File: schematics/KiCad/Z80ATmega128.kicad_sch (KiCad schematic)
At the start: 89 parts, among them J1 AVR-ISP-6, J2 Serial I/O, J3 DC 5V, J4 DC 5V, J5 Z80[1..20], J6 Micro_SD_Card_Det_Hirose_DM3AT, J7 Z80[21..40], SW1 RESET, SW2 POWER, U1 74HC08, U10 74HC32, U11 74HC4050, U12 LP2950-3.3, U13 74HC74, U2 74HC04, U3 74HC125, U4 74AC573, U5 74HC574, U6 74HC125, U7 74HC244, U8 74HC245, U9 74HC32, Y1 16MHz, Y2 8MHz

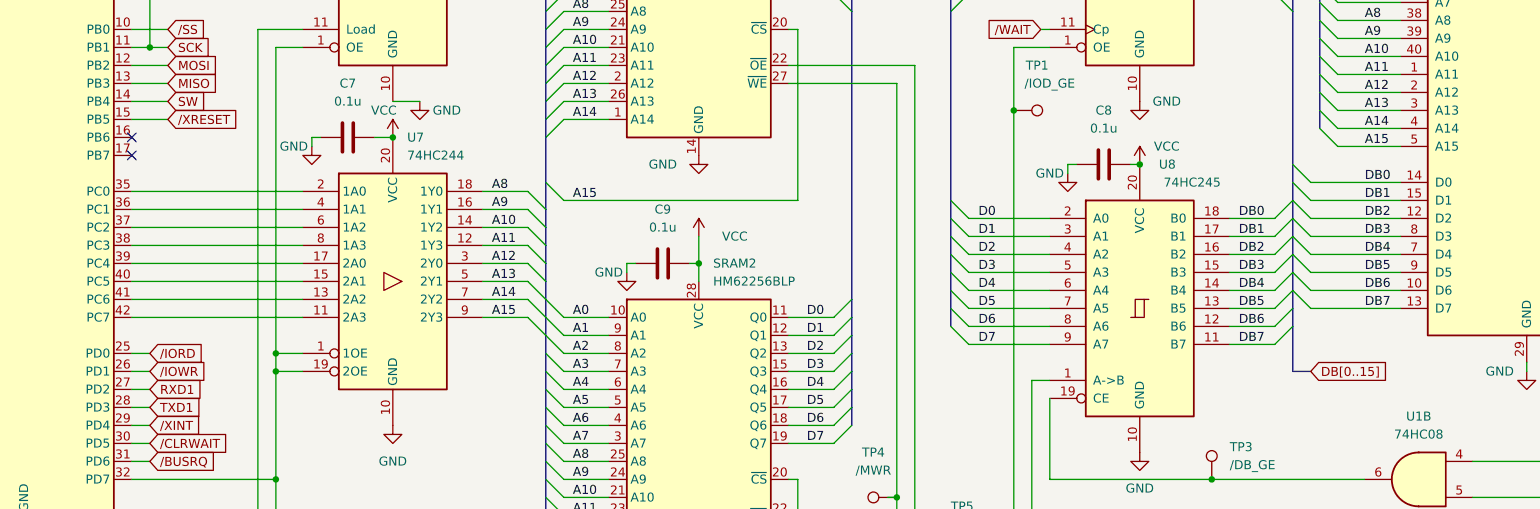
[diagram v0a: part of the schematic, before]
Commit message: Update schematics for Z80 /HALT and /NMI.
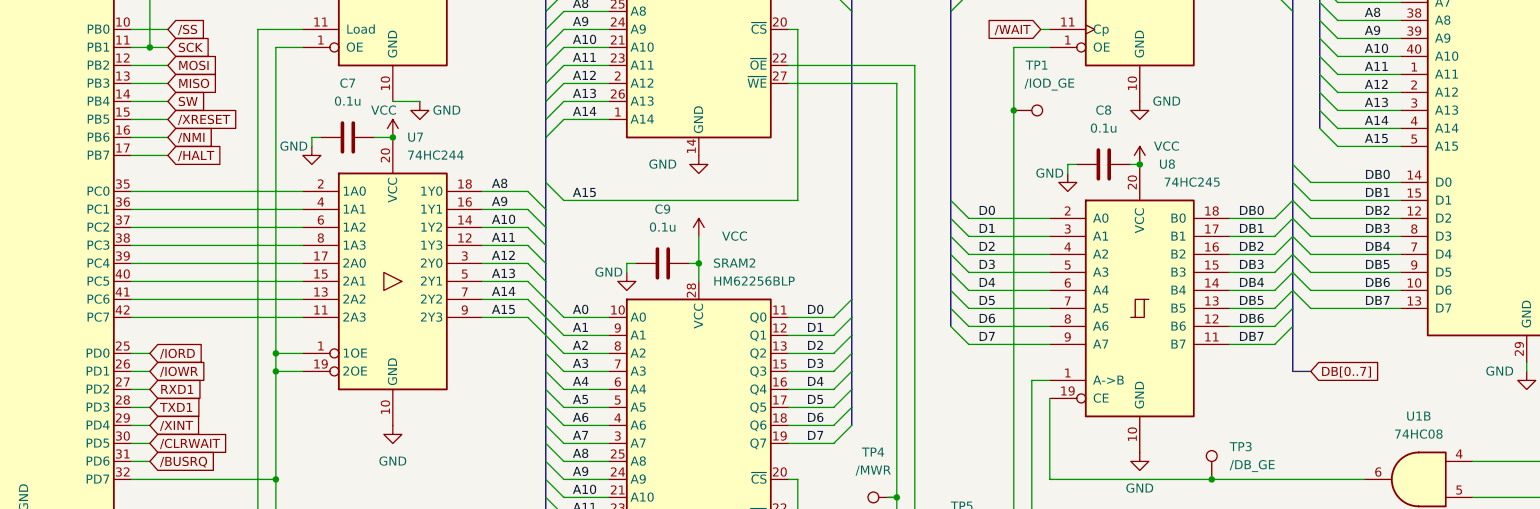
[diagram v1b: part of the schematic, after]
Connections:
- net /HALT: now also CPU2.17 (PB7)
- net /NMI: now also CPU2.16 (PB6)
- no-connect marks 17 -> 15
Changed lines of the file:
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@@
   )
   (no_connect (at 289.56 259.08))
-  (no_connect (at 135.89 86.36))
-  (no_connect (at 135.89 83.82))
   (no_connect (at 105.41 78.74))
   (no_connect (at 289.56 273.05))
@@
     (stroke (width 0) (type default) (color 0 0 0 0))
   )
+  (wire (pts (xy 135.89 83.82) (xy 140.97 83.82))
+    (stroke (width 0) (type default) (color 0 0 0 0))
+  )
   (wire (pts (xy 261.62 205.74) (xy 261.62 212.09))
     (stroke (width 0) (type default) (color 0 0 0 0))
@@
     (stroke (width 0) (type default) (color 0 0 0 0))
   )
+  (wire (pts (xy 135.89 86.36) (xy 140.97 86.36))
+    (stroke (width 0) (type default) (color 0 0 0 0))
+  )
   (wire (pts (xy 394.97 26.67) (xy 394.97 30.48))
     (stroke (width 0) (type default) (color 0 0 0 0))
@@
     )
   )
+  (global_label "{slash}NMI" (shape input) (at 140.97 83.82 0) (fields_autoplaced)
+    (effects (font (size 1.27 1.27)) (justify left))
+    (property "シート間のリファレンス" "${INTERSHEET_REFS}" (id 0) (at 148.1002 83.7406 0)
+      (effects (font (size 1.27 1.27)) (justify left) hide)
+    )
+  )
   (global_label "{slash}IORD" (shape input) (at 138.43 114.3 0) (fields_autoplaced)
     (effects (font (size 1.27 1.27)) (justify left))
@@
     )
   )
-  (global_label "DB[0..15]" (shape input) (at 302.26 116.84 0) (fields_autoplaced)
+  (global_label "DB[0..7]" (shape input) (at 302.26 116.84 0) (fields_autoplaced)
     (effects (font (size 1.27 1.27)) (justify left))
-    (property "シート間のリファレンス" "${INTERSHEET_REFS}" (id 0) (at 313.7445 116.7606 0)
+    (property "シート間のリファレンス" "${INTERSHEET_REFS}" (id 0) (at 312.535 116.7606 0)
       (effects (font (size 1.27 1.27)) (justify left) hide)
     )
@@
       (effects (font (size 1.27 1.27)) (justify left) hide)
     )
+  )
+  (global_label "{slash}HALT" (shape input) (at 140.97 86.36 0) (fields_autoplaced)
+    (effects (font (size 1.27 1.27)) (justify left))
+    (property "シート間のリファレンス" "${INTERSHEET_REFS}" (id 0) (at 149.1283 86.2806 0)
+      (effects (font (size 1.27 1.27)) (justify left) hide)
+    )

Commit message: Update schematics.
Separate reset and SD card interface as different layer.
Power on/manual reset are isolated from ISP /RST for stability.
XMEM /RD(PG1) and /WR(PG0) were swapped.
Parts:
- removed C22: 0.1u, Capacitor_THT:C_Disc_D3.8mm_W2.6mm_P2.50mm, symbol Device:C
- removed C6: 1u, Capacitor_THT:CP_Radial_Tantal_D5.0mm_P2.50mm, symbol Device:C
- removed D2: 1N4148, Diode_THT:D_DO-35_SOD27_P7.62mm_Horizontal, symbol Diode:1N4148
- removed D4: SD Access, LED_THT:LED_D3.0mm, symbol Device:LED
- removed J6: Micro_SD_Card_Det_Hirose_DM3AT, Connector_Card:microSD_HC_Hirose_DM3AT-SF-PEJM5, symbol Connector:Micro_SD_Card_Det_Hirose_DM3AT
- removed R15, R16, R17, R2, R21, R3: 10K, Resistor_THT:R_Axial_DIN0204_L3.6mm_D1.6mm_P7.62mm_Horizontal, symbol Device:R
- removed R22: 1K, Resistor_THT:R_Axial_DIN0204_L3.6mm_D1.6mm_P7.62mm_Horizontal, symbol Device:R
- removed R4: 100, Resistor_THT:R_Axial_DIN0204_L3.6mm_D1.6mm_P7.62mm_Horizontal, symbol Device:R
- removed SW1: RESET, Button_Switch_THT:SW_PUSH_6mm_H7.3mm, symbol Switch:SW_Push
- removed unit 4 of U1
- removed U11: 74HC4050, Package_DIP:DIP-16_W7.62mm, symbol 4xxx:4050
- added JP1: Disable Z80, Connector_PinHeader_2.54mm:PinHeader_1x03_P2.54mm_Vertical, symbol Jumper:Jumper_3_Open
- added R1: 10K, Resistor_THT:R_Axial_DIN0204_L3.6mm_D1.6mm_P7.62mm_Horizontal, symbol Device:R
- D2: renamed from D1; value DMA -> Z80 active
- J4: renamed from J5; symbol Connector:Conn_01x20_Male -> Connector:Conn_01x20_Pin
- J6: renamed from J7; symbol Connector:Conn_01x20_Male -> Connector:Conn_01x20_Pin
- SRAM1, SRAM2: footprint Package_DIP:DIP-28_W15.24mm -> Package_DIP:DIP-28_W15.24mm_Socket
- U1: renamed from U3; footprint Package_DIP:DIP-14_W7.62mm -> Package_DIP:DIP-14_W7.62mm_Socket
- U10: footprint Package_DIP:DIP-14_W7.62mm -> Package_DIP:DIP-14_W7.62mm_Socket
- U11: renamed from U13; footprint Package_DIP:DIP-14_W7.62mm -> Package_DIP:DIP-14_W7.62mm_Socket
- U2: renamed from U4; footprint Package_DIP:DIP-20_W7.62mm -> Package_DIP:DIP-20_W7.62mm_Socket
- U3: renamed from U5; footprint Package_DIP:DIP-20_W7.62mm -> Package_DIP:DIP-20_W7.62mm_Socket
- U4: renamed from U2; footprint Package_DIP:DIP-14_W7.62mm -> Package_DIP:DIP-16_W7.62mm_Socket
- U5: renamed from U6; footprint Package_DIP:DIP-14_W7.62mm -> Package_DIP:DIP-14_W7.62mm_Socket
- U6: renamed from U7; footprint Package_DIP:DIP-20_W7.62mm -> Package_DIP:DIP-20_W7.62mm_Socket
- U7: renamed from U8; footprint Package_DIP:DIP-20_W7.62mm -> Package_DIP:DIP-20_W7.62mm_Socket
- U8: renamed from U9; footprint Package_DIP:DIP-14_W7.62mm -> Package_DIP:DIP-14_W7.62mm_Socket
- U9: renamed from U1; footprint Package_DIP:DIP-14_W7.62mm -> Package_DIP:DIP-14_W7.62mm_Socket
- renumbered C13 to C10, C14 to C11, C11 to C12, C12 to C13, C15 to C14, C16 to C15, C17 to C16, C18 to C17, C19 to C18, C20 to C19, C21 to C20, C7 to C6, C8 to C7, C9 to C8, C10 to C9, D3 to D1, J4 to J5, JP1 to JP2, R13 to R10, R14 to R11, R20 to R12, R18 to R13, R19 to R14, R1 to R15, R5 to R2, R6 to R3, R7 to R4, R8 to R5, R9 to R6, R10 to R7, R11 to R8, R12 to R9, SW2 to SW1, TP12 to TP10, TP9 to TP12, TP7 to TP6, TP6 to TP7, TP10 to TP8, TP8 to TP9
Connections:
- net GND: now also JP1.1 (A)
- net VCC: now also R1.1
- net /BUSRQ: now also JP1.3 (B); no longer CPU1.25 (~{BUSRQ}), R9.2
- net /RD: now also U5.12; no longer U5.9
- net /WR: now also U5.9; no longer U5.12
- net at SRAM1.22 (~{OE}), SRAM2.22 (~{OE}), TP5.1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: now also U5.11; no longer U5.8
- net at SRAM1.27 (~{WE}), SRAM2.27 (~{WE}), TP4.1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: now also U5.8; no longer U5.11
- net Reset//ISP_RST: now reaches J1.5 (~{RST}), U1.13, U4.5
- net Reset//ISP_RST: now also R1.2; no longer CPU2.20 (~{RESET})
- net /RESET renamed /Z80_RESET
- net /XRESET renamed Reset//Z80_SWRST
- new net: CPU1.25 (~{BUSRQ}), JP1.2 (C), R9.2
- new net Reset//AVR_RST: CPU2.20 (~{RESET})
- no-connect marks 15 -> 10
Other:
- added sheet Reset (Reset.kicad_sch)
- added sheet SD_Card_Interface (SD_Card.kicad_sch)
- title: (none) -> Z80 / ATmega128 Board
- moved on the sheet: C10, C11, C12, C13, C9, D1, D2, J3, J4, J5, J6, JP2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

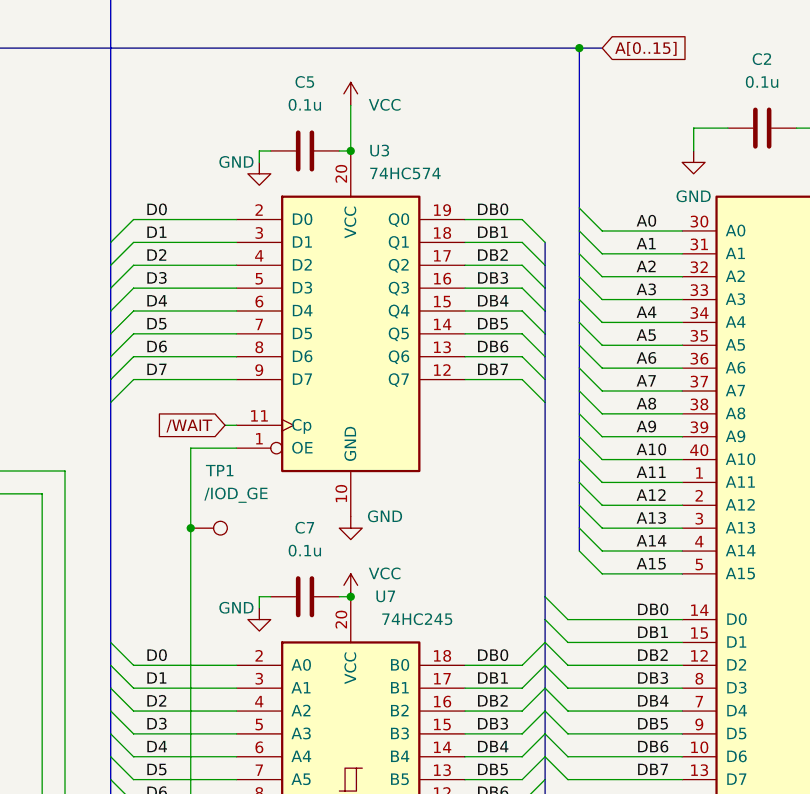
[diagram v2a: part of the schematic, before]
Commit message: 74HC574 and 245 are changed to 74HCT.
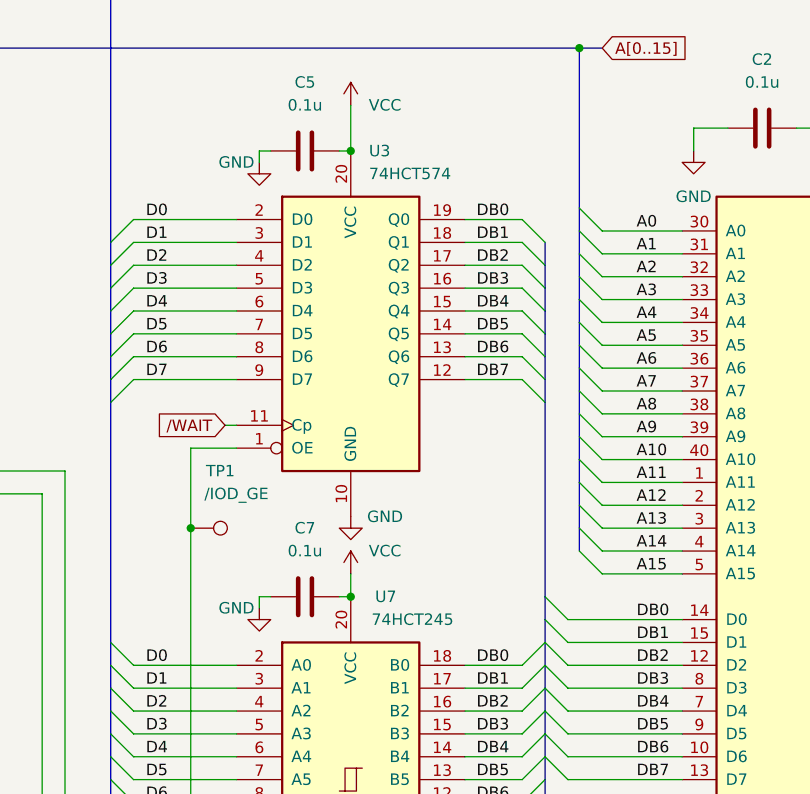
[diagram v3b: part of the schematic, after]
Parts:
- U3: value 74HC574 -> 74HCT574
- U7: value 74HC245 -> 74HCT245
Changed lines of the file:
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@@
     (stroke (width 0) (type default))
   )
+  (wire (pts (xy 278.13 85.09) (xy 278.13 87.63))
+    (stroke (width 0) (type default))
+  )
   (bus (pts (xy 91.44 109.22) (xy 91.44 111.76))
     (stroke (width 0) (type default))
@@
       (effects (font (size 1.27 1.27)) (justify right))
     )
-    (property "Value" "74HC245" (at 289.56 90.17 0)
+    (property "Value" "74HCT245" (at 289.56 90.17 0)
       (effects (font (size 1.27 1.27)) (justify right))
     )
@@
       (effects (font (size 1.27 1.27)) hide)
     )
-    (property "Datasheet" "http://www.ti.com/lit/gpn/sn74HC245" (at 278.13 107.95 0)
+    (property "Datasheet" "http://www.ti.com/lit/gpn/sn74HCT245" (at 278.13 107.95 0)
       (effects (font (size 1.27 1.27)) hide)
     )
@@
     )
   )
-  (symbol (lib_id "power:VCC") (at 278.13 87.63 0) (unit 1)
+  (symbol (lib_id "power:VCC") (at 278.13 85.09 0) (unit 1)
     (in_bom yes) (on_board yes) (dnp no)
-    (property "Reference" "#PWR026" (at 278.13 91.44 0)
+    (property "Reference" "#PWR026" (at 278.13 88.9 0)
       (effects (font (size 1.27 1.27)) hide)
     )
-    (property "Value" "VCC" (at 281.94 85.09 0)
+    (property "Value" "VCC" (at 281.94 82.55 0)
       (effects (font (size 1.27 1.27)))
     )
-    (property "Footprint" "" (at 278.13 87.63 0)
+    (property "Footprint" "" (at 278.13 85.09 0)
       (effects (font (size 1.27 1.27)) hide)
     )
-    (property "Datasheet" "" (at 278.13 87.63 0)
+    (property "Datasheet" "" (at 278.13 85.09 0)
       (effects (font (size 1.27 1.27)) hide)
     )
@@
       (effects (font (size 1.27 1.27)) (justify left))
     )
-    (property "Value" "74HC574" (at 280.1494 40.64 0)
+    (property "Value" "74HCT574" (at 280.1494 40.64 0)
       (effects (font (size 1.27 1.27)) (justify left))
     )
@@
       (effects (font (size 1.27 1.27)) hide)
     )
-    (property "Datasheet" "http://www.ti.com/lit/gpn/sn74HC574" (at 278.13 58.42 0)
+    (property "Datasheet" "http://www.ti.com/lit/gpn/sn74HCT574" (at 278.13 58.42 0)
       (effects (font (size 1.27 1.27)) hide)
     )

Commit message: Changed USB power line connection.
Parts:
- removed J2: Serial I/O, Connector_PinHeader_2.54mm:PinHeader_1x05_P2.54mm_Vertical, symbol Connector:Screw_Terminal_01x05
- added J2: Serial0, Connector_PinHeader_2.54mm:PinHeader_1x06_P2.54mm_Vertical, symbol Connector:Conn_01x06_Pin
- added J3: Serial1, Connector_PinHeader_2.54mm:PinHeader_1x06_P2.54mm_Vertical, symbol Connector:Conn_01x06_Pin
- U4: footprint Package_DIP:DIP-16_W7.62mm_Socket -> Package_DIP:DIP-14_W7.62mm_Socket
- renumbered J3 to J4, J4 to J5, J5 to J6, J6 to J7
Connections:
- net GND: now also J2.6 (Pin_6), J3.6 (Pin_6)
- net RXD1: now also J3.2 (Pin_2)
- net TXD1: now also J3.3 (Pin_3)
- net at U5.2: now also J2.2 (Pin_2)
- net at U5.6: now also J2.3 (Pin_3)
- net VBUS: now reaches JP2.2 (C), SW1.2 (B)
- net VBUS: now also J2.4 (Pin_4), J3.4 (Pin_4)
- no-connect marks 10 -> 14
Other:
- moved on the sheet: C12, C13, C9, D1, J4, J6, JP2, R11, SW1, TP12, TP7, TP9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

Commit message: Update Reset circuit and Serial interface
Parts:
- removed C12: 1u, Capacitor_THT:CP_Radial_Tantal_D5.0mm_P2.50mm, symbol Device:C
- removed C13: 1u, Capacitor_THT:CP_Radial_Tantal_D5.0mm_P2.50mm, symbol Device:C_Polarized
- removed J2: Serial0, Connector_PinHeader_2.54mm:PinHeader_1x06_P2.54mm_Vertical, symbol Connector:Conn_01x06_Pin
- removed J3: Serial1, Connector_PinHeader_2.54mm:PinHeader_1x06_P2.54mm_Vertical, symbol Connector:Conn_01x06_Pin
- removed TP12: 3.3V, TestPoint:TestPoint_Loop_D2.50mm_Drill1.0mm, symbol Connector:TestPoint
- removed U12: LP2950-3.3, Package_TO_SOT_THT:TO-92_Inline, symbol Regulator_Linear:LP2950-3.3_TO92
- added U10, U5: AE-CH340E-TYPEC, Connector_PinHeader_2.54mm:PinHeader_1x06_P2.54mm_Vertical, symbol 46nori_Library:AE-CH340E-TYPEC
- renumbered C14 to C12, C15 to C13, C16 to C14, C17 to C15, C18 to C16, C19 to C17, C20 to C18, J4 to J2, J6 to J3, J5 to J4, J7 to J5, TP9 to TP8, TP8 to TP9, U9 to U11, U10 to U12, U11 to U13, U5 to U6, U6 to U7, U7 to U8, U8 to U9
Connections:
- net GND: now also U10.6 (GND), U5.6 (GND)
- net RXD1: now also U10.3 (TXD)
- net TXD1: now also U10.2 (RXD)
- net at U6.2: now also U5.3 (TXD)
- net at U6.6: now also U5.2 (RXD)
- net VBUS: no longer names the net of JP2.2 (C), SW1.2 (B)
- net VBUS: now also U10.4 (VCC), U5.4 (VCC)
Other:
- sheet Reset ports: added /ST; removed none
- moved on the sheet: C9, D1, J2, J3, JP2, R11, SW1, TP7, TP8

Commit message: Update schematics.
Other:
- company: (none) -> By 46nori
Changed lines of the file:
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@@
   (title_block
     (title "Z80 / ATmega128 Board")
-    (date "2023-04-14")
+    (date "2023-05-03")
+    (company "By 46nori")
   )
   (junction (at 389.89 163.83) (diameter 0) (color 0 0 0 0)
@@
     (stroke (width 0) (type default))
   )
+  (wire (pts (xy 34.29 146.05) (xy 43.18 146.05))
+    (stroke (width 0) (type default))
+  )
   (wire (pts (xy 332.74 116.84) (xy 332.74 115.57))
     (stroke (width 0) (type default))
@@
     (stroke (width 0) (type default))
   )
+  (wire (pts (xy 30.48 146.05) (xy 34.29 146.05))
+    (stroke (width 0) (type default))
+  )
   (wire (pts (xy 67.31 116.84) (xy 105.41 116.84))
     (stroke (width 0) (type default))
@@
     (stroke (width 0) (type default))
   )
-  (wire (pts (xy 34.29 146.05) (xy 34.29 149.86))
+  (wire (pts (xy 43.18 146.05) (xy 43.18 149.86))
     (stroke (width 0) (type default))
   )
@@
     (stroke (width 0) (type default))
   )
-  (wire (pts (xy 30.48 146.05) (xy 34.29 146.05))
-    (stroke (width 0) (type default))
-  )
   (wire (pts (xy 142.24 220.98) (xy 142.24 227.33))
     (stroke (width 0) (type default))
@@
     (stroke (width 0) (type default))
   )
+  (text_box "1-2 : Force disable\n2-3 : Enable"
+    (at 383.54 20.32 0) (size 22.86 5.08)
+    (stroke (width 0) (type default))
+    (fill (type none))
+    (effects (font (size 1.27 1.27)) (justify left top))
+  )
+  (text_box "USB/Serial CH0"
+    (at 13.97 114.3 0) (size 17.78 3.81)
+    (stroke (width 0) (type default))
+    (fill (type none))
+    (effects (font (size 1.27 1.27)) (justify top))
+  )
+  (text_box "USB/Serial CH1"
+    (at 13.97 149.86 0) (size 17.78 3.81)
+    (stroke (width 0) (type default))
+    (fill (type none))
+    (effects (font (size 1.27 1.27)) (justify top))
+  )
   (label "D3" (at 231.14 116.84 0) (fields_autoplaced)
     (effects (font (size 1.27 1.27)) (justify left bottom))
@@
     )
   )
-  (symbol (lib_id "power:GND") (at 34.29 149.86 0) (unit 1)
+  (symbol (lib_id "power:GND") (at 43.18 149.86 0) (unit 1)
     (in_bom yes) (on_board yes) (dnp no) (fields_autoplaced)
-    (property "Reference" "#PWR035" (at 34.29 156.21 0)
+    (property "Reference" "#PWR035" (at 43.18 156.21 0)
       (effects (font (size 1.27 1.27)) hide)
     )
-    (property "Value" "GND" (at 34.29 154.94 0)
+    (property "Value" "GND" (at 43.18 154.94 0)
       (effects (font (size 1.27 1.27)))
     )
-    (property "Footprint" "" (at 34.29 149.86 0)
+    (property "Footprint" "" (at 43.18 149.86 0)
       (effects (font (size 1.27 1.27)) hide)
     )
-    (property "Datasheet" "" (at 34.29 149.86 0)
+    (property "Datasheet" "" (at 43.18 149.86 0)
       (effects (font (size 1.27 1.27)) hide)
     )
@@
   (symbol (lib_id "power:PWR_FLAG") (at 38.1 182.88 0) (mirror x) (unit 1)
     (in_bom yes) (on_board yes) (dnp no)
-    (property "Reference" "#FLG01" (at 38.1 184.785 0)
+    (property "Reference" "#FLG02" (at 38.1 184.785 0)
       (effects (font (size 1.27 1.27)) hide)
     )
@@
       (project "Z80ATmega128"
         (path "/8c0ff608-9e5b-458c-8fa7-b9973ff97e88"
-          (reference "#FLG01") (unit 1)
+          (reference "#FLG02") (unit 1)
         )
       )
@@
   (symbol (lib_id "power:PWR_FLAG") (at 68.58 167.64 0) (mirror y) (unit 1)
     (in_bom yes) (on_board yes) (dnp no)
-    (property "Reference" "#FLG02" (at 68.58 165.735 0)
+    (property "Reference" "#FLG01" (at 68.58 165.735 0)
       (effects (font (size 1.27 1.27)) hide)
     )
@@
       (project "Z80ATmega128"
         (path "/8c0ff608-9e5b-458c-8fa7-b9973ff97e88"
-          (reference "#FLG02") (unit 1)
+          (reference "#FLG01") (unit 1)
         )
       )

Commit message: Update RESET circuit using DS1232N.
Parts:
- removed R15: 1K, Resistor_THT:R_Axial_DIN0204_L3.6mm_D1.6mm_P7.62mm_Horizontal, symbol Device:R
- removed SW1: POWER, Button_Switch_THT:SW_Slide_1P2T_CK_OS102011MS2Q, symbol Switch:SW_SPDT
- removed TP1: /IOD_GE, TestPoint:TestPoint_Loop_D2.50mm_Drill1.0mm, symbol Connector:TestPoint
- removed TP10: /CLRWAIT, TestPoint:TestPoint_Loop_D2.50mm_Drill1.0mm, symbol Connector:TestPoint
- removed TP2: /IOWR, TestPoint:TestPoint_Loop_D2.50mm_Drill1.0mm, symbol Connector:TestPoint
- removed TP3: /DB_GE, TestPoint:TestPoint_Loop_D2.50mm_Drill1.0mm, symbol Connector:TestPoint
- removed TP4: /MWR, TestPoint:TestPoint_Loop_D2.50mm_Drill1.0mm, symbol Connector:TestPoint
- removed TP5: /MRD, TestPoint:TestPoint_Loop_D2.50mm_Drill1.0mm, symbol Connector:TestPoint
- removed TP6: /IORD, TestPoint:TestPoint_Loop_D2.50mm_Drill1.0mm, symbol Connector:TestPoint
- removed TP9: /INTRQ, TestPoint:TestPoint_Loop_D2.50mm_Drill1.0mm, symbol Connector:TestPoint
- removed unit 3 of U4
- added C19: 0.1u, Capacitor_THT:C_Disc_D3.8mm_W2.6mm_P2.50mm, symbol Device:C
- added R2: 1K, Resistor_THT:R_Axial_DIN0204_L3.6mm_D1.6mm_P7.62mm_Horizontal, symbol Device:R
- added R3: 10K, Resistor_THT:R_Axial_DIN0204_L3.6mm_D1.6mm_P7.62mm_Horizontal, symbol Device:R
- added SW1: Power, symbol Switch:SW_Push_DPDT
- added U13: 74LS08, Package_DIP:DIP-14_W7.62mm_Socket, symbol 74xx:74LS08
- added unit 3 of U2
- renumbered D2 to D1, D1 to D2, R8 to R10, R9 to R11, R10 to R12, R11 to R13, R12 to R14, R13 to R15, R14 to R16, R2 to R4, R3 to R5, R4 to R6, R5 to R7, R6 to R8, R7 to R9, TP7 to TP1, TP8 to TP2, TP11 to TP3, U11 to U10, U12 to U11, U9 to U12, U13 to U14, U4 to U2, U2 to U3, U3 to U4, U10 to U9
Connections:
- net A15: now also U12.13; no longer SRAM1.20 (~{CS})
- net A7: no longer U12.1
- net GND: now also R12.1, C19.2, U13.12, U13.13, U13.7 (GND); no longer U12.12, U12.13
- net Reset//ISP_RST: now also U2.5
- net Reset//Z80_SWRST: now also R3.2
- net VCC: now also C19.1, R2.2, R3.1, SW1.3 (C), SW1.6 (C), U13.14 (VCC); no longer R12.1
- net /BUSACK: no longer U2.13
- net /IORQ: now also R6.2, U11.10, U11.12; no longer R7.2, U12.2
- net /MREQ: now also R7.2, U13.5; no longer R6.2
- net /RD: now also U13.1
- net /WR: now also U13.2
- net at SRAM2.20 (~{CS}): now also U12.3; no longer U2.4
- net at U5.4 (VCC), U9.4 (VCC): now also SW1.2 (B); no longer JP2.2 (C)
- net at U6.1, U6.4: now also U2.6
- net at CPU1.23 (~{BUSACK}), U1.9: now also R11.2, U2.13; no longer R12.2
- net at CPU1.25 (~{BUSRQ}), JP1.2 (C): now also R12.2; no longer R11.2
- net at U12.11: now also SRAM1.20 (~{CS})
- net at D1.2 (A): now also R2.1
- new net: U12.1, U2.4
- new net: JP2.2 (C), SW1.5 (B)
- new net: U12.12, U12.2, U13.6
- new net: U13.3, U13.4
- no-connect marks 14 -> 15
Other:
- moved on the sheet: C10, C11, C4, C8, D1, J1, JP1, R12, R13, R14, R15, R16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
